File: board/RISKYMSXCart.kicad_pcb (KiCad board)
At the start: 4 copper layers, 71.9 x 55.5 mm, 37 parts, among them CN1 MSX_CART, IC8 LM1117MPX-3.3, J1 Conn_01x02, J2 Conn_01x02, J5 Conn_01x02, J7 USB_1, J8 Conn_01x02, SW1 SW_Push, U1 CH32V307VCT6

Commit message: Rev2 PCB
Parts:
- removed J5: Conn_01x02, Connector_PinHeader_2.54mm:PinHeader_1x02_P2.54mm_Vertical
- removed PWR: PWR, LED_SMD:LED_0805_2012Metric_Pad1.15x1.40mm_HandSolder
- added C12: C, Capacitor_SMD:C_0603_1608Metric_Pad1.08x0.95mm_HandSolder, B.Cu at (118.0, 122.0)
- added C14: C, Capacitor_SMD:C_0603_1608Metric_Pad1.08x0.95mm_HandSolder, B.Cu at (129.5, 116.5)
- added C15: C, Capacitor_SMD:C_0805_2012Metric_Pad1.18x1.45mm_HandSolder, B.Cu at (146.9, 120.2)
- added C16: C, Capacitor_SMD:C_0805_2012Metric_Pad1.18x1.45mm_HandSolder, B.Cu at (150.2, 120.1)
- added D5: PWR, LED_SMD:LED_0805_2012Metric_Pad1.15x1.40mm_HandSolder, F.Cu at (182.4, 112.5)
- added JP1: Jumper_2_Open, Jumper:SolderJumper-2_P1.3mm_Open_RoundedPad1.0x1.5mm, B.Cu at (125.7, 115.7)
- added R9: R, Resistor_SMD:R_0603_1608Metric_Pad0.98x0.95mm_HandSolder, B.Cu at (129.2, 119.9)
- added U2: MCP6001-OT, Package_TO_SOT_SMD:SOT-23-5, B.Cu at (125.5, 119.7)
- added Y1: Crystal, Crystal:Crystal_SMD_5032-2Pin_5.0x3.2mm_HandSoldering, F.Cu at (148.8, 116.9)
- C1, C10, C13, IC8, R3: moved to B.Cu
- C7: value 22uF -> C; footprint tfcart:PANASONIC_B -> Capacitor_SMD:C_1206_3216Metric_Pad1.33x1.80mm_HandSolder; moved to B.Cu
- R2: value 10k -> R
- moved R2 24.5 mm to (124.7, 122.2)
- moved J1 6.29 mm to (126.5, 96.7)
- moved R1 6.29 mm to (123.5, 96.7)
- moved R8 6.29 mm to (156.4, 109.4), turned to 90 degrees
- moved C13 4.09 mm to (176.2, 111.7), turned to 0 degrees
- moved R6 3.35 mm to (154.2, 116.8)
- moved R7 2.90 mm to (155.8, 116.8)
- moved R5 2.80 mm to (149.1, 112.8), turned to 180 degrees
- moved C1 1.31 mm to (180.7, 106.3), turned to -90 degrees
- moved D1 1.23 mm to (150.1, 112.8)
- moved D2 1.23 mm to (152.1, 112.8)
- moved D3 1.23 mm to (154.2, 112.8)
- moved D4 1.23 mm to (156.2, 112.8)
- moved IC8 1.05 mm to (175.3, 105.8), turned to 180 degrees
- moved C7 0.94 mm to (176.2, 98.1), turned to 180 degrees
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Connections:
- R2 pad 1: GND -> Net-(JP1-B)
- R2 pad 2: /BOOT1 -> Net-(U2--)
- U1 pad 12: unconnected-(U1-OSC_IN-Pad12) -> Net-(U1-OSC_IN)
- U1 pad 13: unconnected-(U1-OSC_OUT-Pad13) -> Net-(U1-OSC_OUT)
- U1 pad 29: /SCC_AUD -> /SCC_OUT
- U1 pad 37: /BOOT1 -> GND
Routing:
- net /SCC_AUD: track 55.7 -> 5.93 mm, vias 1 -> 0
- net /BOOT1: track 44.3 -> 0.00 mm, vias 6 -> 0
- net /SCC_OUT: track 0.00 -> 35.5 mm, vias 0 -> 1
- net Net-(JP1-B): track 0.00 -> 19.7 mm
- net +3.3V: track 43.2 -> 26.1 mm, vias 18 -> 19
- net Net-(U1-OSC_OUT): track 0.00 -> 14.1 mm, vias 0 -> 1
- net Net-(U1-OSC_IN): track 0.00 -> 10.5 mm, vias 0 -> 1
- net /A14: track 35.3 -> 43.2 mm
- net Net-(U2--): track 0.00 -> 6.96 mm
- net /A12: track 36.0 -> 42.7 mm
- net Net-(U2-+): track 0.00 -> 6.10 mm
- net /BOOT0: track 35.0 -> 29.5 mm
- net GND: track 32.2 -> 37.6 mm, vias 23 -> 27
- net +5V: track 48.8 -> 52.7 mm, vias 6 -> 5
- net Net-(D2-A): track 0.00 -> 3.67 mm
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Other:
- board text added: "Rev.2"
- board text removed: "B1"
- board text removed: "Rev.1"

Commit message: Initial version 2.1
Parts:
- removed C15, C16: C, Capacitor_SMD:C_0805_2012Metric_Pad1.18x1.45mm_HandSolder
- removed D2, D3, D4: LED, LED_SMD:LED_0805_2012Metric_Pad1.15x1.40mm_HandSolder
- removed JP1: Jumper_2_Open, Jumper:SolderJumper-2_P1.3mm_Open_RoundedPad1.0x1.5mm
- removed R6, R7, R8: 2.2k, Resistor_SMD:R_0603_1608Metric_Pad0.98x0.95mm_HandSolder
- removed SW1: SW_Push, Button_Switch_SMD:SW_SPST_Omron_B3FS-105xP
- removed Y1: Crystal, Crystal:Crystal_SMD_5032-2Pin_5.0x3.2mm_HandSoldering
- added C17: C, Capacitor_SMD:C_0603_1608Metric_Pad1.08x0.95mm_HandSolder, B.Cu at (128.8, 120.0)
- added C18: C, Capacitor_SMD:C_0603_1608Metric_Pad1.08x0.95mm_HandSolder, B.Cu at (132.6, 118.0)
- added C19: C, Capacitor_SMD:C_0603_1608Metric_Pad1.08x0.95mm_HandSolder, B.Cu at (132.6, 116.5)
- added C20: C, Capacitor_SMD:C_0603_1608Metric_Pad1.08x0.95mm_HandSolder, B.Cu at (132.6, 115.0)
- added R10: R, Resistor_SMD:R_0603_1608Metric_Pad0.98x0.95mm_HandSolder, B.Cu at (130.8, 113.4)
- moved D1 34.0 mm to (134.1, 82.8)
- moved D5 31.5 mm to (173.6, 82.4)
- moved R5 31.4 mm to (133.2, 85.8)
- moved R3 29.0 mm to (176.5, 83.8), turned to 180 degrees
- moved R2 5.55 mm to (128.8, 118.5)
- moved U2 4.97 mm to (128.8, 116.0)
- moved C14 4.78 mm to (124.8, 115.6)
- moved R9 3.43 mm to (132.6, 119.5), turned to 180 degrees
- moved C12 3.42 mm to (120.8, 120.0), turned to 180 degrees
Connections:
- C14 pad 1: /SCC_OUT -> Net-(U2-+)
- C14 pad 2: Net-(U2-+) -> GND
- D1 pad 1: /LED1 -> /LEDFLASH
- U1 pad 12: Net-(U1-OSC_IN) -> unconnected-(U1-OSC_IN-Pad12)
- U1 pad 13: Net-(U1-OSC_OUT) -> unconnected-(U1-OSC_OUT-Pad13)
- U1 pad 23: /LED1 -> unconnected-(U1-PA0/WKUP/ADC0-Pad23)
- U1 pad 24: /LED2 -> unconnected-(U1-PA1/ADC1-Pad24)
- U1 pad 25: /LED3 -> unconnected-(U1-PA2/ADC2-Pad25)
- U1 pad 26: /LED4 -> unconnected-(U1-PA3/ADC3-Pad26)
- U1 pad 67: /BTN1 -> /LEDFLASH
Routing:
- net /BTN1: track 28.6 -> 0.00 mm, vias 2 -> 0
- net /LEDFLASH: track 0.00 -> 24.7 mm, vias 0 -> 2
- net Net-(U1-OSC_OUT): track 14.1 -> 0.00 mm, vias 1 -> 0
- net +3.3V: track 26.1 -> 38.0 mm, vias 19 -> 15
- net Net-(U1-OSC_IN): track 10.5 -> 0.00 mm, vias 1 -> 0
- net Net-(C12-Pad1): track 19.7 -> 9.53 mm
- net /SCC_OUT: track 35.5 -> 28.1 mm
- net /LED4: track 5.02 -> 0.00 mm
- net /SCC_AUD: track 5.93 -> 10.2 mm
- net /LED1: track 3.77 -> 0.00 mm
- net Net-(D2-A): track 3.67 -> 0.00 mm, vias 1 -> 0
- net Net-(D4-A): track 3.55 -> 0.00 mm, vias 1 -> 0
- net +5V: track 52.7 -> 56.0 mm, vias 5 -> 6
- net /LED3: track 3.18 -> 0.00 mm
- net /LED2: track 2.87 -> 0.00 mm
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
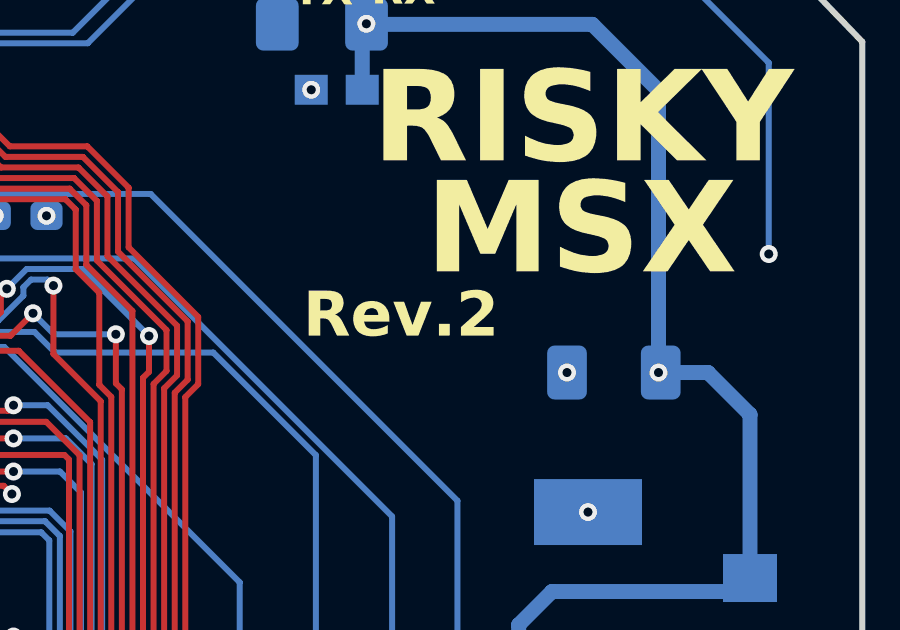
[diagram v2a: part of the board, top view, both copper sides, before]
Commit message: v2.1.8 Rev2.1 PCB Design change BOM change https://github.com/arkadiuszmakarenko/RISKYMSX/issues/7 fix https://github.com/arkadiuszmakarenko/RISKYMSX/issues/6 fix FLashLED added.
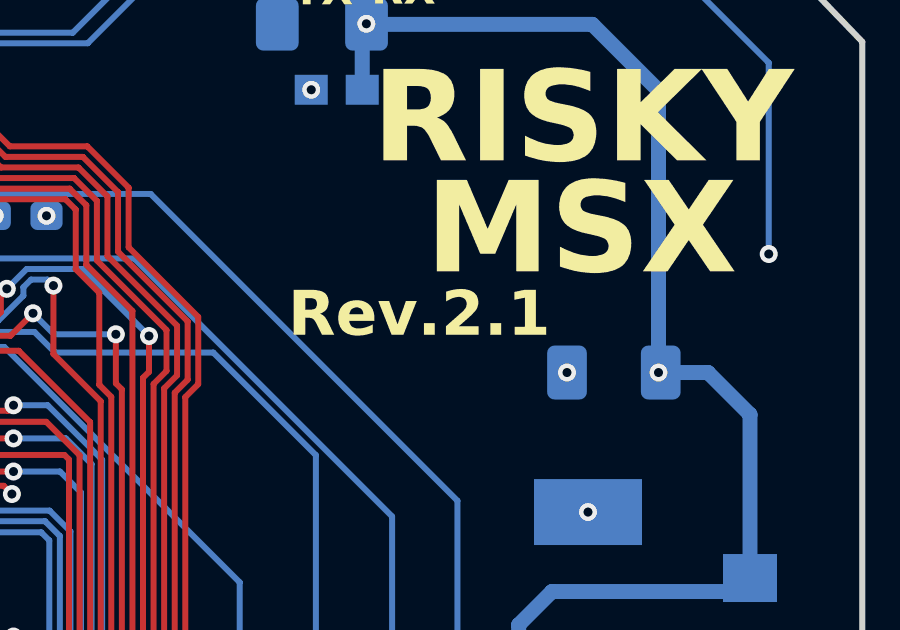
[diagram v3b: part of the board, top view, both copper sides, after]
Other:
- board text added: "Rev.2.1"
- board text removed: "Rev.2"
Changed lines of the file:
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@@
 		)
 	)
-	(gr_text "Rev.2"
-		(at 165.8 97.05 0)
+	(gr_text "Rev.2.1"
+		(at 165.3 97.025 0)
 		(layer "F.SilkS")
 		(effects

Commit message: Specify confirmed values in BoM, schematic and PCB, fix minor csv bom issues, add .gitignore (#10)
* schematic: add confirmed values for components with missing values

Signed-off-by: Albert Herranz <albert_herranz@yahoo.es>

* pcb: update values from schematic

Signed-off-by: Albert Herranz <albert_herranz@yahoo.es>

* kicad: add interactive BoM

Signed-off-by: Albert Herranz <albert_herranz@yahoo.es>

* add .gitignore

Signed-off-by: Albert Herranz <albert_herranz@yahoo.es>

* csv bom: fix duplicate C14

Signed-off-by: Albert Herranz <albert_herranz@yahoo.es>

* csv bom: match footprint of C7 in BoM to that of the PCB

Signed-off-by: Albert Herranz <albert_herranz@yahoo.es>

* csv bom: fix fuse name

Signed-off-by: Albert Herranz <albert_herranz@yahoo.es>

* csv bom: add missing R10

Signed-off-by: Albert Herranz <albert_herranz@yahoo.es>

* csv bom: rename leds with board names

Signed-off-by: Albert Herranz <albert_herranz@yahoo.es>

---------

Signed-off-by: Albert Herranz <albert_herranz@yahoo.es>
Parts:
- C10, C11, C19, C2, C4, C5, C6, C7, C8: value C -> 100nF
- C12, C20: value C -> 4.7uF
- C14, C17: value C -> 1nF
- C18: value C -> 1uF
- C9: value 0.1μF -> 100nF
- F2: value Fuse -> 0.5A
- R1: value 10k -> 10K
- R10, R2, R4, R9: value R -> 10K
- R3: value 10k -> 220
- R5: value 2.2k -> 220
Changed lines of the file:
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@@
 			)
 		)
-		(property "Value" "R"
+		(property "Value" "10K"
 			(at 0 -1.43 0)
 			(layer "B.Fab")
@@
 			)
 		)
-		(property "Value" "2.2k"
+		(property "Value" "220"
 			(at -0.1 -4.2 0)
 			(layer "B.Fab")
@@
 			)
 		)
-		(property "Value" "C"
+		(property "Value" "1nF"
 			(at 0 -1.43 180)
 			(layer "B.Fab")
@@
 			)
 		)
-		(property "Value" "C"
+		(property "Value" "100nF"
 			(at 0 -1.43 90)
 			(layer "B.Fab")
@@
 			)
 		)
-		(property "Value" "C"
+		(property "Value" "1uF"
 			(at 0 -1.43 180)
 			(layer "B.Fab")
@@
 			)
 		)
-		(property "Value" "C"
+		(property "Value" "100nF"
 			(at 0.1625 -1.45 90)
 			(layer "B.Fab")
@@
 			)
 		)
-		(property "Value" "C"
+		(property "Value" "100nF"
 			(at 0 -1.43 90)
 			(layer "B.Fab")
@@
 			)
 		)
-		(property "Value" "C"
+		(property "Value" "100nF"
 			(at 0 -1.43 0)
 			(layer "B.Fab")
@@
 			)
 		)
-		(property "Value" "0.1μF"
+		(property "Value" "100nF"
 			(at 0.0375 -1.525 90)
 			(layer "B.Fab")
@@
 			)
 		)
-		(property "Value" "C"
+		(property "Value" "100nF"
 			(at 0 -1.85 0)
 			(layer "B.Fab")
@@
 			)
 		)
-		(property "Value" "C"
+		(property "Value" "4.7uF"
 			(at 0 -1.43 180)
 			(layer "B.Fab")
@@
 			)
 		)
-		(property "Value" "10k"
+		(property "Value" "10K"
 			(at 0 -1.43 0)
 			(layer "B.Fab")
@@
 			)
 		)
-		(property "Value" "C"
+		(property "Value" "100nF"
 			(at 3.3 1.7 0)
 			(layer "B.Fab")
@@
 			)
 		)
-		(property "Value" "C"
+		(property "Value" "100nF"
 			(at -0.1 1.5 90)
 			(layer "B.Fab")
@@
 			)
 		)
-		(property "Value" "10k"
+		(property "Value" "220"
 			(at -0.635 -1.905 0)
 			(layer "B.Fab")
@@
 			)
 		)
-		(property "Value" "R"
+		(property "Value" "10K"
 			(at 0 -1.43 180)
 			(layer "B.Fab")
@@
 			)
 		)
-		(property "Value" "C"
+		(property "Value" "4.7uF"
 			(at 0 -1.43 0)
 			(layer "B.Fab")
@@
 			)
 		)
-		(property "Value" "C"
+		(property "Value" "1nF"
 			(at 0 -1.43 90)
 			(layer "B.Fab")
@@
 			)
 		)
-		(property "Value" "R"
+		(property "Value" "10K"
 			(at -0.15 -1.6 0)
 			(layer "B.Fab")
@@
 			)
 		)
-		(property "Value" "C"
+		(property "Value" "100nF"
 			(at 0 -1.43 180)
 			(layer "B.Fab")
@@
 			)
 		)
-		(property "Value" "C"
+		(property "Value" "100nF"
 			(at 0 -1.43 90)
 			(layer "B.Fab")
@@
 			)
 		)
-		(property "Value" "Fuse"
+		(property "Value" "0.5A"
 			(at -0.6 -1.85 0)
 			(layer "B.Fab")
@@
 			)
 		)
-		(property "Value" "R"
+		(property "Value" "10K"
 			(at 0 -1.43 90)
 			(layer "B.Fab")
